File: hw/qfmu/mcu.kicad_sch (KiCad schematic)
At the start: 0 parts

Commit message: feat: add material list and create library dir
Create a spreadsheet to annotate BOM and include symbols in lib/
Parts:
- added J1: Conn_02x06_Counter_Clockwise, Connector_PinHeader_2.54mm:PinHeader_2x06_P2.54mm_Vertical, symbol Connector_Generic:Conn_02x06_Counter_Clockwise
- added U1: EFM32GG11B120F2048GQ64, TQFP64_10X10_SIL, symbol EFM32GG11B120F2048GQ64:EFM32GG11B120F2048GQ64
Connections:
- new net +3.3V: J1.1 (Pin_1)
- new net GND: J1.10 (Pin_10), J1.11 (Pin_11), J1.12 (Pin_12), J1.7 (Pin_7), J1.8 (Pin_8), J1.9 (Pin_9)
- new net RESETN: J1.2 (Pin_2), U1.20 (RESETn)
- new net SWDCLK/TCLK: J1.6 (Pin_6), U1.49 (PF0)
- new net SWDIO/TMS: J1.5 (Pin_5), U1.50 (PF1)
- new net SWO/TDO: J1.4 (Pin_4), U1.51 (PF2)
- new net TDI: J1.3 (Pin_3), U1.54 (PF5)
- no-connect marks 0 -> 49

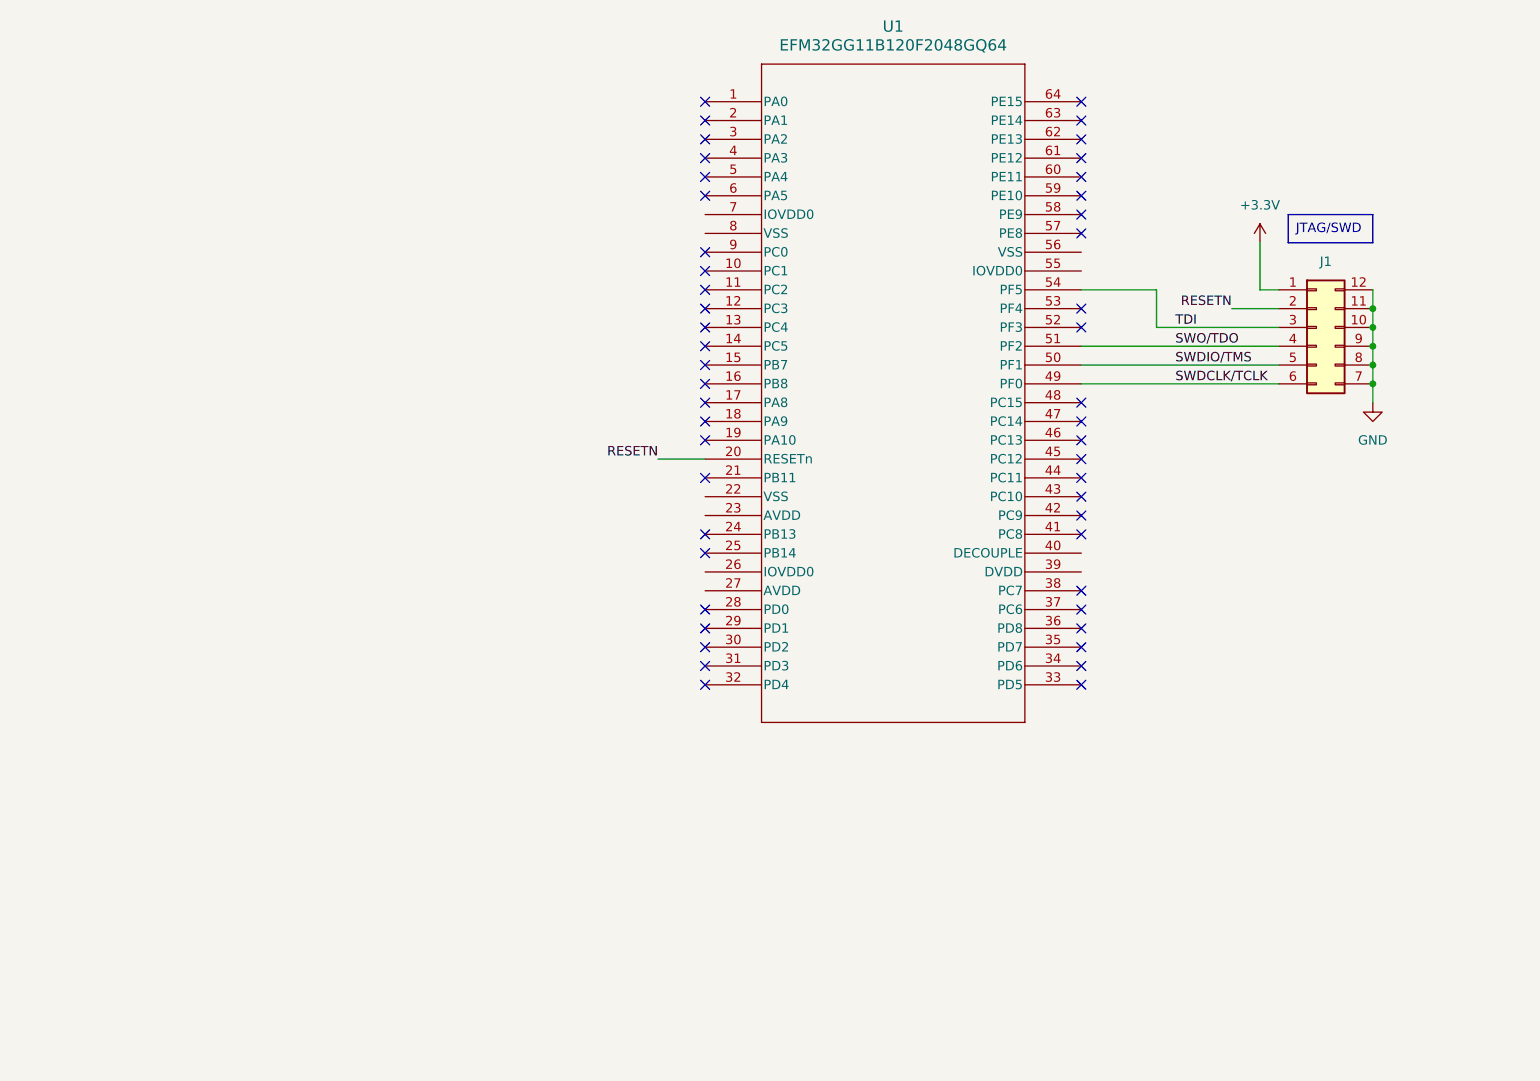
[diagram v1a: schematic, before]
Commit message: feat: add MCU, basic motor structure, sensors and power
Initialize basic structure for the motor, sensor and power sheets.
Update material list (mats.ods) with more components to be used.
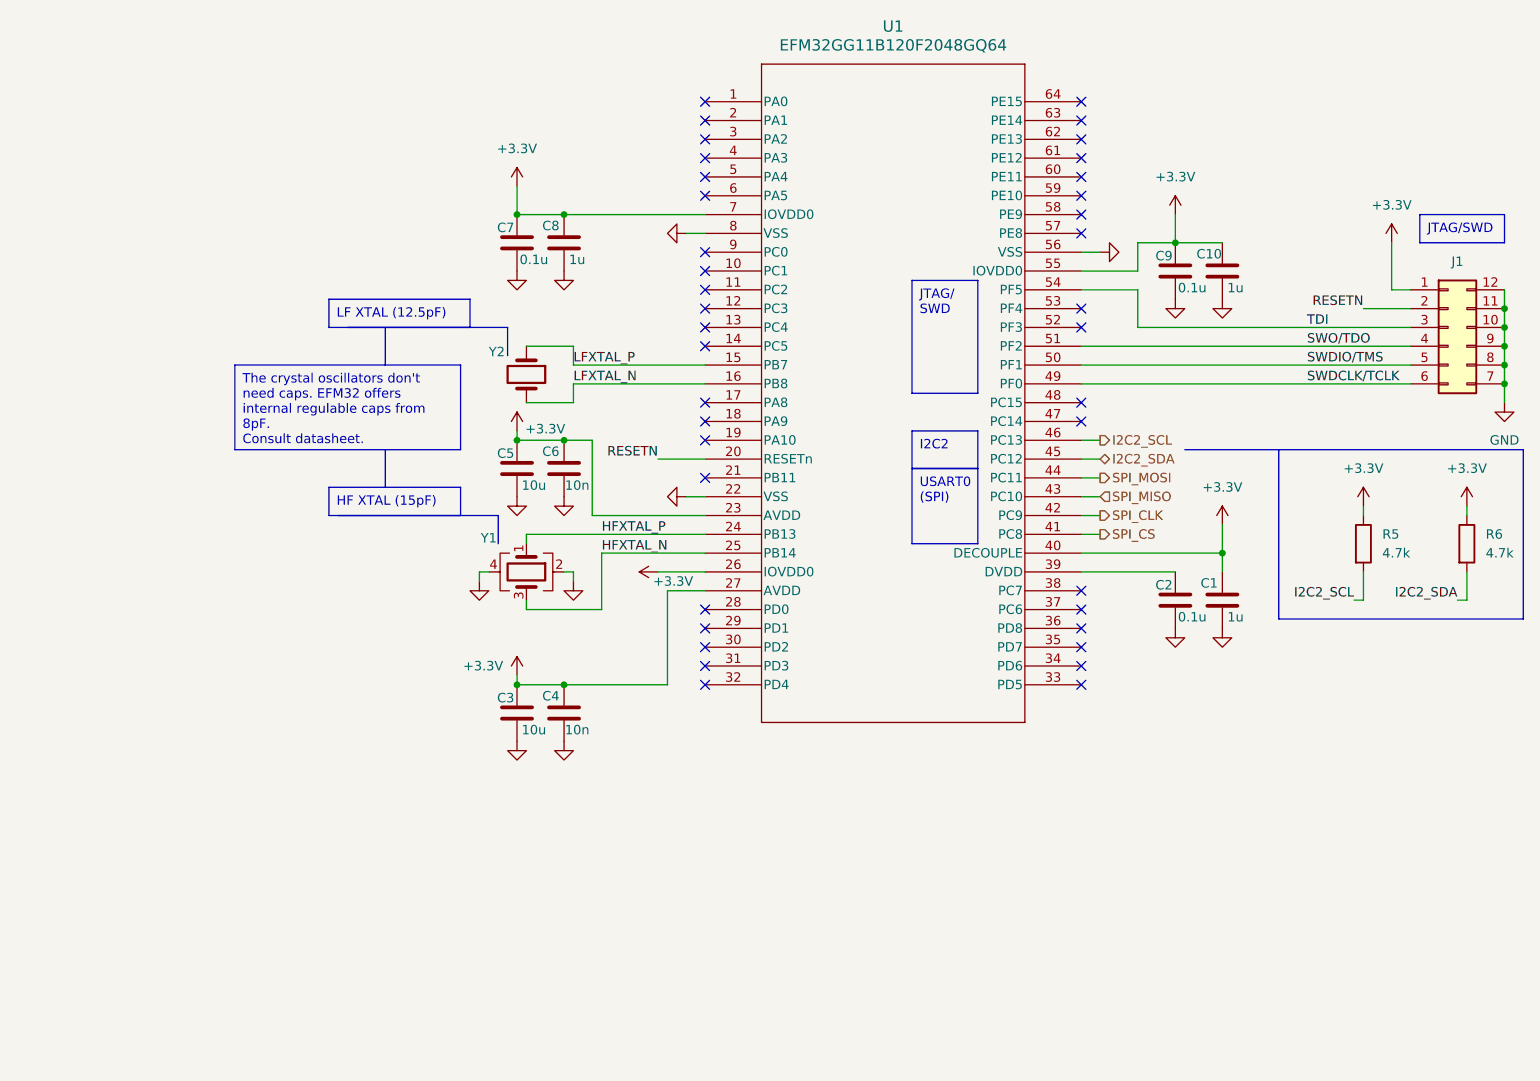
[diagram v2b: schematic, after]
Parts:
- added C1, C10, C8: 1u, Capacitor_SMD:C_0805_2012Metric_Pad1.18x1.45mm_HandSolder, symbol Device:C
- added C2, C7, C9: 0.1u, Capacitor_SMD:C_0805_2012Metric_Pad1.18x1.45mm_HandSolder, symbol Device:C
- added C3, C5: 10u, Capacitor_SMD:C_0805_2012Metric_Pad1.18x1.45mm_HandSolder, symbol Device:C
- added C4, C6: 10n, Capacitor_SMD:C_0805_2012Metric_Pad1.18x1.45mm_HandSolder, symbol Device:C
- added R5, R6: 4.7k, Resistor_SMD:R_0805_2012Metric_Pad1.20x1.40mm_HandSolder, symbol Device:R
- added Y1: Crystal_GND24, Crystal:Crystal_SMD_3225-4Pin_3.2x2.5mm_HandSoldering, symbol Device:Crystal_GND24
- added Y2: Crystal, Crystal:Crystal_SMD_EuroQuartz_EQ161-2Pin_3.2x1.5mm_HandSoldering, symbol Device:Crystal
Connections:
- net +3.3V: now also U1.23 (AVDD), U1.26 (IOVDD0), U1.27 (AVDD), U1.40 (DECOUPLE), U1.55 (IOVDD0), U1.7 (IOVDD0), C1.1, C10.1, C3.1, C4.1, C5.1, C6.1, C7.1, C8.1, C9.1, R5.1, R6.1
- net GND: now also U1.22 (VSS), U1.56 (VSS), U1.8 (VSS), C1.2, C10.2, C2.2, C3.2, C4.2, C5.2, C6.2, C7.2, C8.2, C9.2, Y1.2, Y1.4
- net LFXTAL_P: now reaches U1.15 (PB7)
- net LFXTAL_P: now also Y2.1
- net LFXTAL_N: now reaches U1.16 (PB8)
- net LFXTAL_N: now also Y2.2
- net HFXTAL_P: now reaches U1.24 (PB13)
- net HFXTAL_P: now also Y1.1
- net HFXTAL_N: now reaches U1.25 (PB14)
- net HFXTAL_N: now also Y1.3
- net at U1.39 (DVDD): now also C2.1
- net SPI_CS: now reaches U1.41 (PC8)
- net SPI_CLK: now reaches U1.42 (PC9)
- net SPI_MISO: now reaches U1.43 (PC10)
- net SPI_MOSI: now reaches U1.44 (PC11)
- net I2C2_SDA: now reaches U1.45 (PC12)
- net I2C2_SDA: now also R6.2
- net I2C2_SCL: now reaches U1.46 (PC13)
- net I2C2_SCL: now also R5.2
- no-connect marks 49 -> 39
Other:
- moved on the sheet: J1

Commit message: feat: add new BLDC controler and RF section
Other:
- company: Daniel Pérez -> Daniel Enrique Pérez Díaz
- title: (none) -> Quincy FMU
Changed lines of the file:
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@@
 	(paper "A4")
 	(title_block
-		(date "2024-09-10")
+		(title "Quincy FMU")
+		(date "2024-09-28")
 		(rev "0")
-		(company "Daniel Pérez")
+		(company "Daniel Enrique Pérez Díaz")
+		(comment 1 "Flight Management Unit for the Quincy Quadcopter project.")
 	)
 	(junction

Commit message: feat: finish motors, RF and power monitor
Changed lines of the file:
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@@
+		)
+	)
+	(hierarchical_label "IMU_INT_GY1"
+		(shape input)
+		(at 196.85 146.05 180)
+		(fields_autoplaced yes)
+		(effects
+			(font
+				(size 1.27 1.27)
+			)
+			(justify right)
+		)
+	)
+	(hierarchical_label "MON_SDA"
+		(shape bidirectional)
+		(at 196.85 160.02 180)
+		(fields_autoplaced yes)
+		(effects
+			(font
+				(size 1.27 1.27)
+			)
+			(justify right)
 		)
 	)
@@
 			)
 			(justify left)
+		)
+	)
+	(hierarchical_label "IMU_INT_AC1"
+		(shape input)
+		(at 196.85 143.51 180)
+		(fields_autoplaced yes)
+		(effects
+			(font
+				(size 1.27 1.27)
+			)
+			(justify right)
+		)
+	)
+	(hierarchical_label "TX_ASK"
+		(shape output)
+		(at 196.85 138.43 180)
+		(fields_autoplaced yes)
+		(effects
+			(font
+				(size 1.27 1.27)
+			)
+			(justify right)
+		)
+	)
+	(hierarchical_label "ANT_MODE"
+		(shape output)
+		(at 196.85 135.89 180)
+		(fields_autoplaced yes)
+		(effects
+			(font
+				(size 1.27 1.27)
+			)
+			(justify right)
 		)
 	)
@@
 		)
 	)
+	(hierarchical_label "RF_DEMOD"
+		(shape input)
+		(at 196.85 140.97 180)
+		(fields_autoplaced yes)
+		(effects
+			(font
+				(size 1.27 1.27)
+			)
+			(justify right)
+		)
+	)
+	(hierarchical_label "DCHG"
+		(shape input)
+		(at 196.85 154.94 180)
+		(fields_autoplaced yes)
+		(effects
+			(font
+				(size 1.27 1.27)
+			)
+			(justify right)
+		)
+	)
+	(hierarchical_label "MON_SCL"
+		(shape output)
+		(at 196.85 157.48 180)
+		(fields_autoplaced yes)
+		(effects
+			(font
+				(size 1.27 1.27)
+			)
+			(justify right)
+		)
+	)
+	(hierarchical_label "MON_RST_SHUT"
+		(shape output)
+		(at 196.85 149.86 180)
+		(fields_autoplaced yes)
+		(effects
+			(font
+				(size 1.27 1.27)
+			)
+			(justify right)
+		)
+	)
 	(hierarchical_label "SPI_CLK"
 		(shape output)
@@
 		)
 	)
+	(hierarchical_label "DDSG"
+		(shape input)
+		(at 196.85 152.4 180)
+		(fields_autoplaced yes)
+		(effects
+			(font
+				(size 1.27 1.27)
+			)
+			(justify right)
+		)
+	)
+	(hierarchical_label "MON_ALERT"
+		(shape bidirectional)
+		(at 196.85 162.56 180)
+		(fields_autoplaced yes)
+		(effects
+			(font
+				(size 1.27 1.27)
+			)
+			(justify right)
+		)
+	)

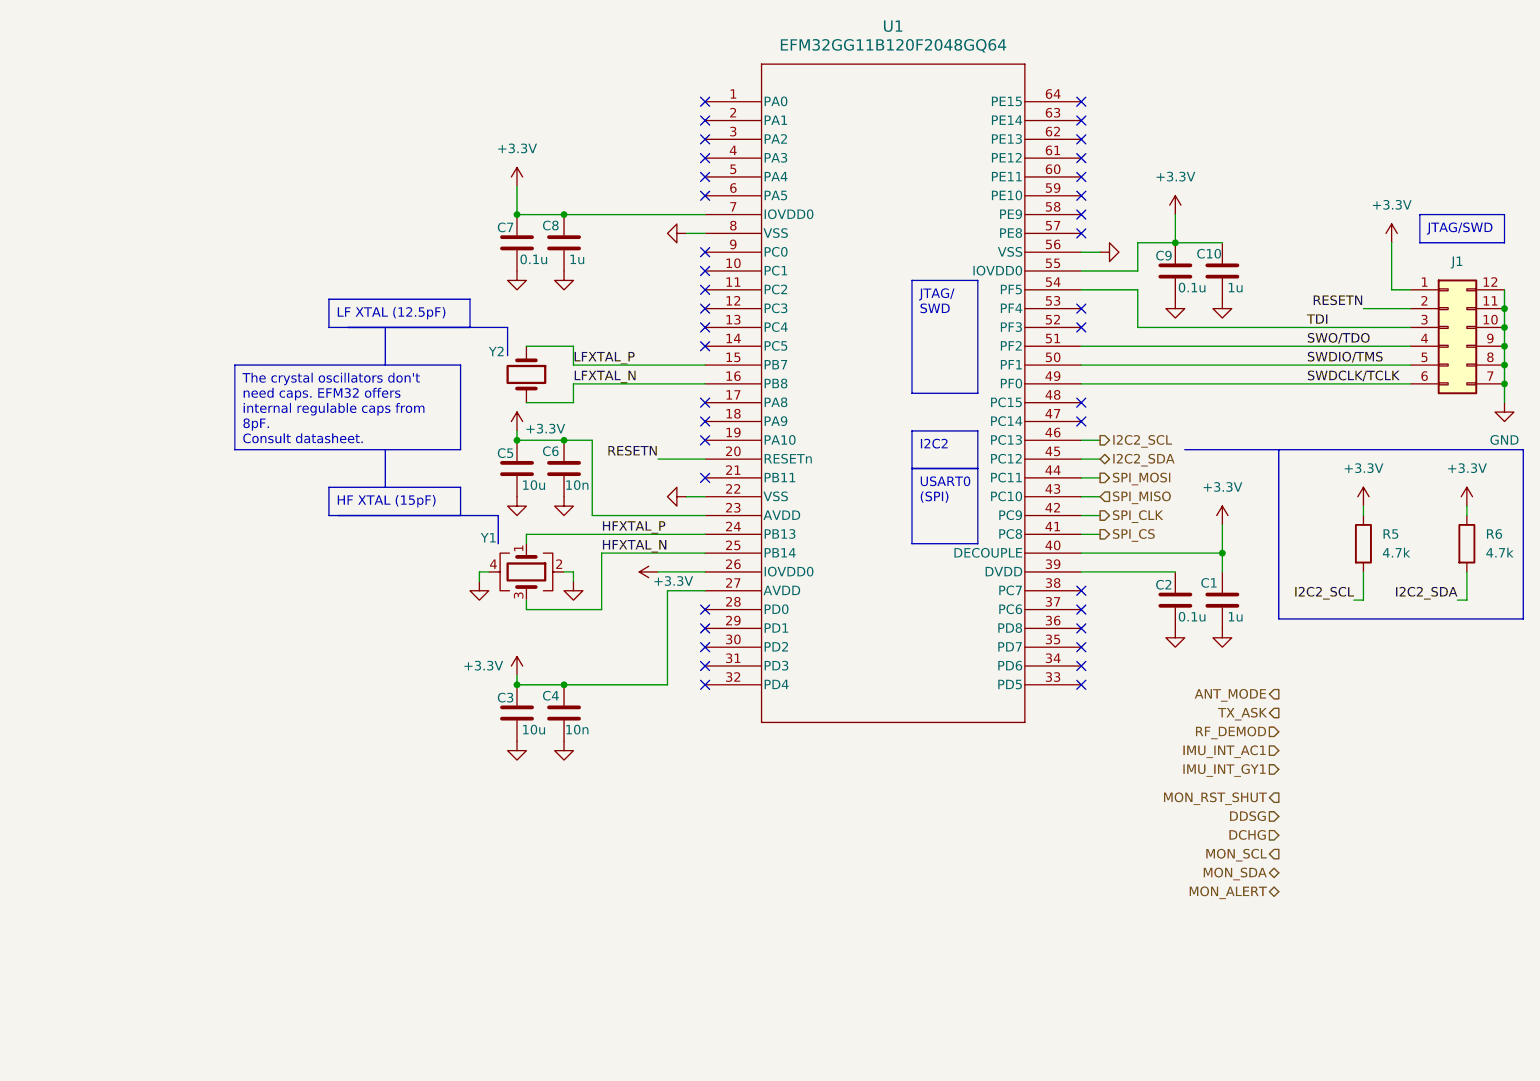
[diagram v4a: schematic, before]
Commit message: feat: start PCB design, define board outline and basic placement
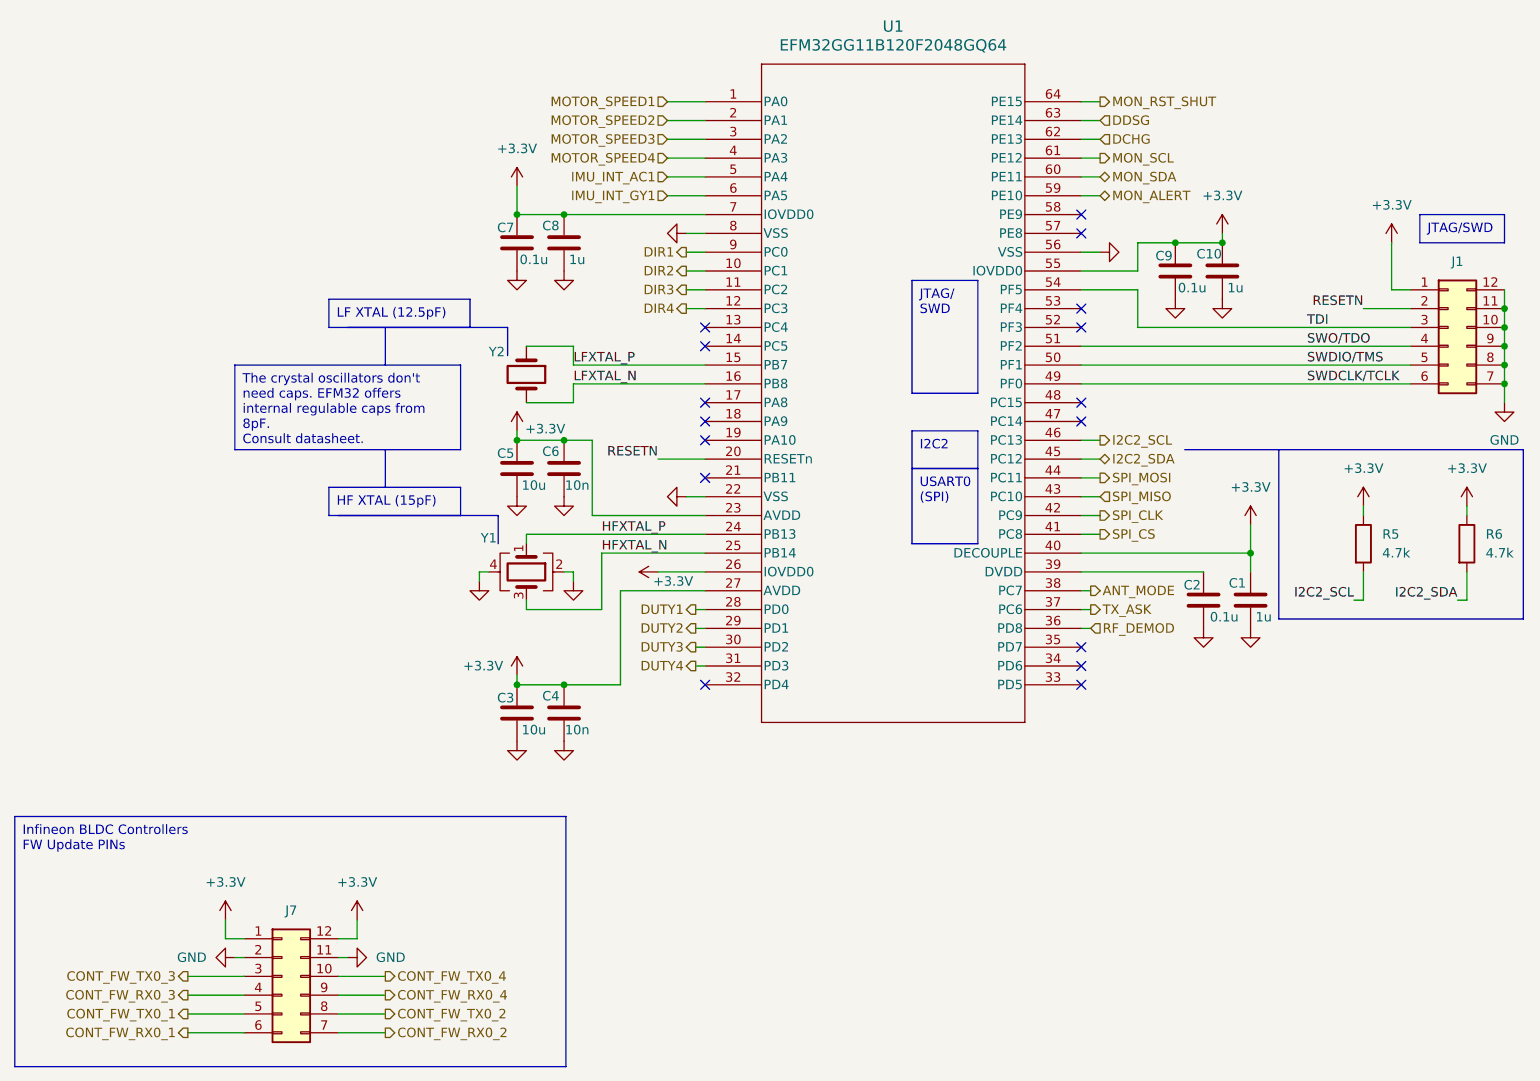
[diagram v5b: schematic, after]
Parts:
- added J7: Conn_02x06_Counter_Clockwise, Connector_PinHeader_2.54mm:PinHeader_2x06_P2.54mm_Vertical, symbol Connector_Generic:Conn_02x06_Counter_Clockwise
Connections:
- net +3.3V: now also J7.1 (Pin_1), J7.12 (Pin_12)
- net ANT_MODE: now also U1.38 (PC7)
- net DCHG: now also U1.62 (PE13)
- net DDSG: now also U1.63 (PE14)
- net GND: now also J7.11 (Pin_11), J7.2 (Pin_2)
- net IMU_INT_AC1: now also U1.5 (PA4)
- net IMU_INT_GY1: now also U1.6 (PA5)
- net MON_ALERT: now also U1.59 (PE10)
- net MON_RST_SHUT: now also U1.64 (PE15)
- net MON_SCL: now also U1.61 (PE12)
- net MON_SDA: now also U1.60 (PE11)
- net RF_DEMOD: now also U1.36 (PD8)
- net TX_ASK: now also U1.37 (PC6)
- net MOTOR_SPEED1: now reaches U1.1 (PA0)
- net DIR2: now reaches U1.10 (PC1)
- net DIR3: now reaches U1.11 (PC2)
- net DIR4: now reaches U1.12 (PC3)
- net MOTOR_SPEED2: now reaches U1.2 (PA1)
- net DUTY1: now reaches U1.28 (PD0)
- net DUTY2: now reaches U1.29 (PD1)
- net MOTOR_SPEED3: now reaches U1.3 (PA2)
- net DUTY3: now reaches U1.30 (PD2)
- net DUTY4: now reaches U1.31 (PD3)
- net MOTOR_SPEED4: now reaches U1.4 (PA3)
- net DIR1: now reaches U1.9 (PC0)
- new net CONT_FW_RX0_1: J7.6 (Pin_6)
- new net CONT_FW_RX0_2: J7.7 (Pin_7)
- new net CONT_FW_RX0_3: J7.4 (Pin_4)
- new net CONT_FW_RX0_4: J7.9 (Pin_9)
- new net CONT_FW_TX0_1: J7.5 (Pin_5)
- new net CONT_FW_TX0_2: J7.8 (Pin_8)
- new net CONT_FW_TX0_3: J7.3 (Pin_3)
- new net CONT_FW_TX0_4: J7.10 (Pin_10)
- no-connect marks 39 -> 16
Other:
- moved on the sheet: C1, C2
